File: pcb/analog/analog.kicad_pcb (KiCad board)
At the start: 2 copper layers, 70 x 70 mm, 65 parts, among them J1 USB_C_Receptacle_USB2.0, SW1 SW_Push, SW2 SW_Push, U1 SRV05-4, U2 XC6206P332MR, U3 DRV5056A3xDBZxQ1, U4 DRV5056A3xDBZxQ1, U5 DRV5056A3xDBZxQ1, U6 74AHCT1G125, U7 74AHCT1G125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

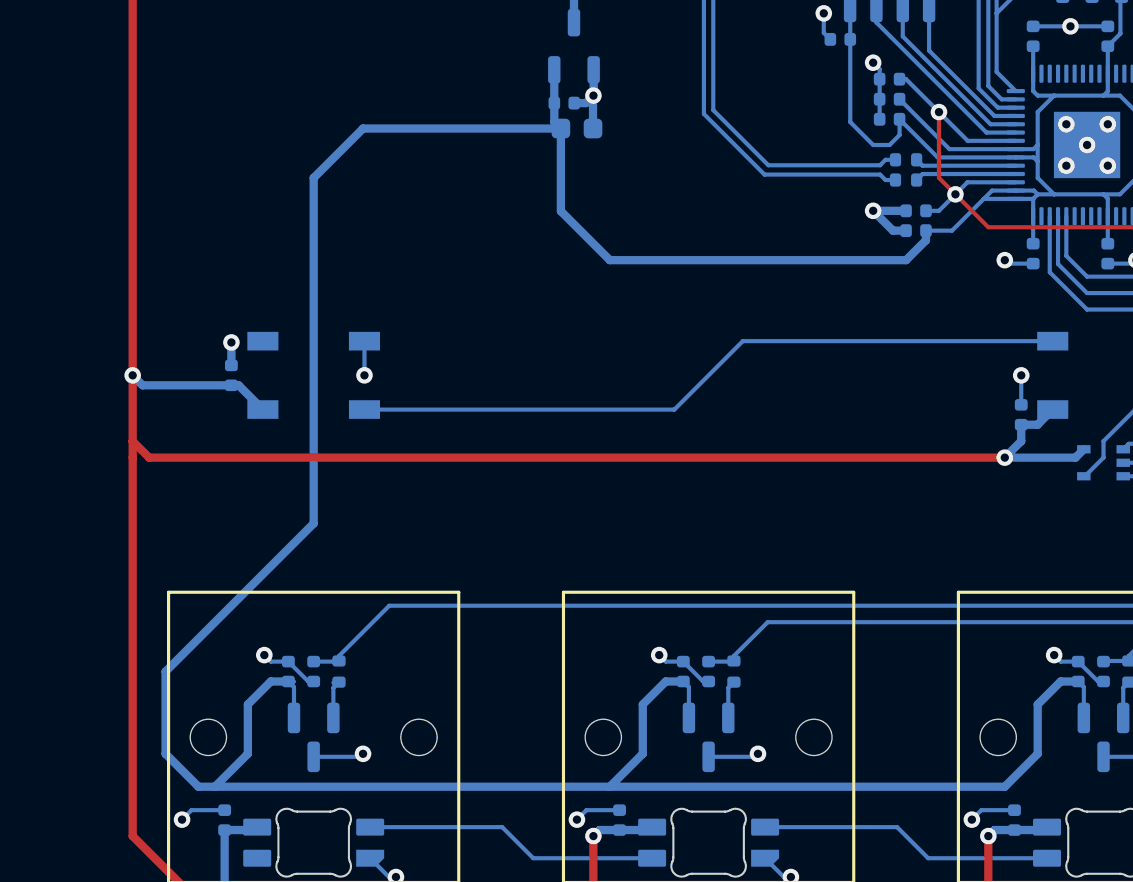
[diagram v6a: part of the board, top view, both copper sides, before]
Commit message: refactor: route analog +3v3 without going underneath LEDs just realised that it may cause some noise in the supply.
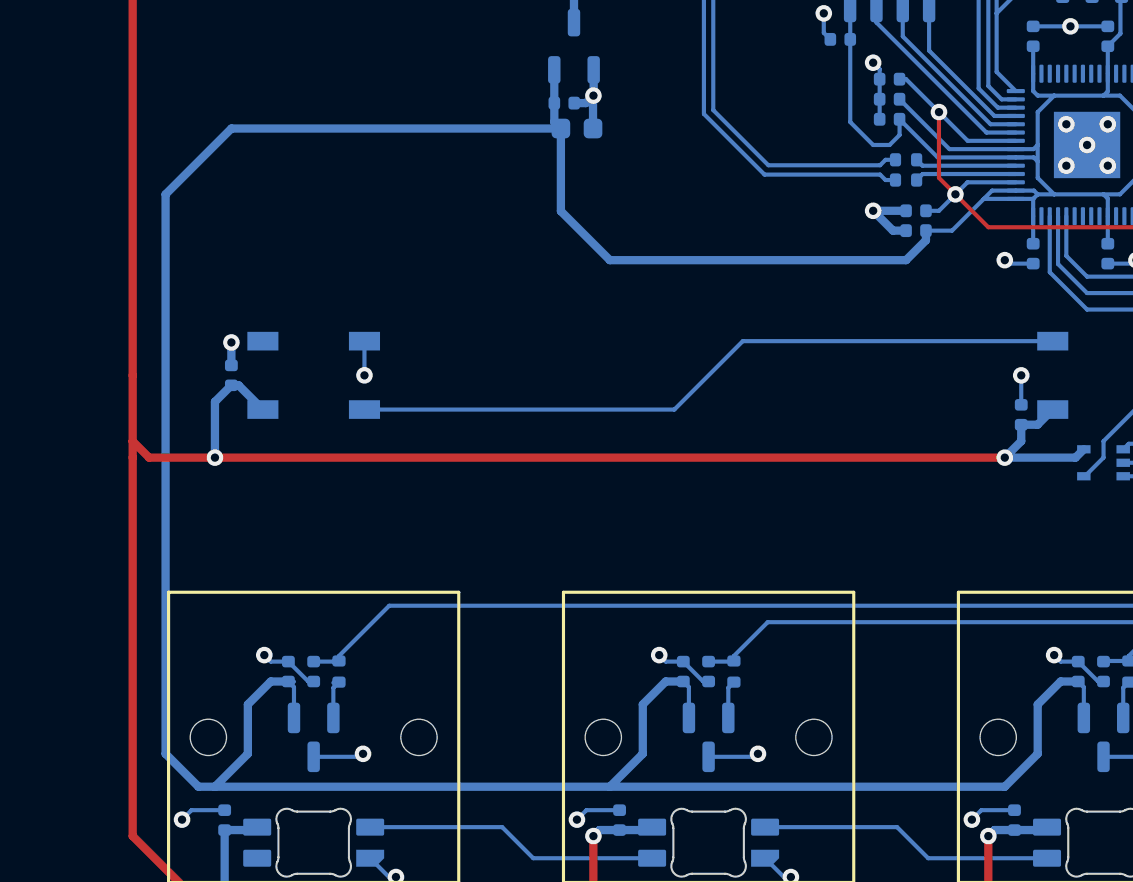
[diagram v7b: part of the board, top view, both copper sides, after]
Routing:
- net +3V3: track 212.8 -> 216.5 mm
- net +5V: track 212.3 -> 211.2 mm
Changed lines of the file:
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@@
     (stroke (width 0.1) (type default)) (layer "Edge.Cuts"))
   (segment (start 43.35625 37.665143) (end 43.358258 37.667151) (width 0.4) (layer "B.Cu") (net 1))
-  (segment (start 43.675 38.89375) (end 34.13125 38.89375) (width 0.4) (layer "B.Cu") (net 1))
   (segment (start 65.61875 42.2875) (end 64.075 42.2875) (width 0.2) (layer "B.Cu") (net 1))
   (segment (start 58.7375 39.6875) (end 57.632335 38.582335) (width 0.2) (layer "B.Cu") (net 1))
-  (segment (start 24.60625 69.05625) (end 26.19375 70.64375) (width 0.4) (layer "B.Cu") (net 1))
   (segment (start 59.53125 39.6875) (end 58.7375 39.6875) (width 0.2) (layer "B.Cu") (net 1))
-  (segment (start 31.75 57.94375) (end 24.60625 65.0875) (width 0.4) (layer "B.Cu") (net 1))
   (segment (start 66.675 38.1) (end 66.675 39.6875) (width 0.2) (layer "B.Cu") (net 1))
   (segment (start 30.8 67.325) (end 30.8 65.837505) (width 0.2) (layer "B.Cu") (net 1))
@@
   (segment (start 60.325 45.24375) (end 61.285 44.28375) (width 0.4) (layer "B.Cu") (net 1))
   (segment (start 70.05625 36.25) (end 70.05625 34.925) (width 0.2) (layer "B.Cu") (net 1))
+  (segment (start 26.19375 70.64375) (end 26.9875 70.64375) (width 0.4) (layer "B.Cu") (net 1))
   (segment (start 66.45625 36.25) (end 66.45625 34.925) (width 0.2) (layer "B.Cu") (net 1))
   (segment (start 71.6375 39.8875) (end 71.4375 39.6875) (width 0.2) (layer "B.Cu") (net 1))
   (segment (start 65.61875 40.2875) (end 61.851075 40.2875) (width 0.2) (layer "B.Cu") (net 1))
+  (segment (start 43.675 38.89375) (end 27.78125 38.89375) (width 0.4) (layer "B.Cu") (net 1))
   (segment (start 66.675 41.275) (end 67.46875 42.06875) (width 0.2) (layer "B.Cu") (net 1))
   (segment (start 71.4375 39.6875) (end 71.4375 38.1) (width 0.2) (layer "B.Cu") (net 1))
@@
   (segment (start 66.675 37.30625) (end 67.46875 37.30625) (width 0.2) (layer "B.Cu") (net 1))
   (segment (start 69.85 37.30625) (end 67.46875 37.30625) (width 0.2) (layer "B.Cu") (net 1))
+  (segment (start 27.78125 38.89375) (end 24.60625 42.06875) (width 0.4) (layer "B.Cu") (net 1))
   (segment (start 70.05625 36.25) (end 70.05625 37.1) (width 0.2) (layer "B.Cu") (net 1))
   (segment (start 65.61875 40.2875) (end 66.48125 40.2875) (width 0.2) (layer "B.Cu") (net 1))
@@
   (segment (start 65.61875 39.8875) (end 62.417962 39.8875) (width 0.2) (layer "B.Cu") (net 1))
   (segment (start 30.8 65.837505) (end 30.529995 65.5675) (width 0.2) (layer "B.Cu") (net 1))
-  (segment (start 31.75 41.275) (end 31.75 57.94375) (width 0.4) (layer "B.Cu") (net 1))
   (segment (start 62.417962 39.8875) (end 60.01125 37.480788) (width 0.2) (layer "B.Cu") (net 1))
   (segment (start 70.05625 42.275) (end 69.85 42.06875) (width 0.2) (layer "B.Cu") (net 1))
@@
   (segment (start 66.45625 43.125) (end 66.45625 44.45) (width 0.2) (layer "B.Cu") (net 1))
   (segment (start 67.46875 42.06875) (end 69.85 42.06875) (width 0.2) (layer "B.Cu") (net 1))
+  (segment (start 24.60625 69.05625) (end 26.19375 70.64375) (width 0.4) (layer "B.Cu") (net 1))
   (segment (start 66.48125 40.2875) (end 66.675 40.48125) (width 0.2) (layer "B.Cu") (net 1))
   (segment (start 64.075 42.2875) (end 62.543453 43.819047) (width 0.2) (layer "B.Cu") (net 1))
-  (segment (start 26.19375 70.64375) (end 26.9875 70.64375) (width 0.4) (layer "B.Cu") (net 1))
   (segment (start 67.46875 37.30625) (end 66.675 38.1) (width 0.2) (layer "B.Cu") (net 1))
   (segment (start 28.575 69.05625) (end 28.575 66.675) (width 0.4) (layer "B.Cu") (net 1))
@@
   (segment (start 68.890937 67.315937) (end 68.9 67.325) (width 0.2) (layer "B.Cu") (net 1))
   (segment (start 43.358258 38.577008) (end 43.675 38.89375) (width 0.4) (layer "B.Cu") (net 1))
-  (segment (start 24.60625 65.0875) (end 24.60625 69.05625) (width 0.4) (layer "B.Cu") (net 1))
   (segment (start 66.45625 42.2875) (end 66.675 42.06875) (width 0.2) (layer "B.Cu") (net 1))
+  (segment (start 24.60625 42.06875) (end 24.60625 69.05625) (width 0.4) (layer "B.Cu") (net 1))
   (segment (start 64.475 41.8875) (end 64.075 42.2875) (width 0.2) (layer "B.Cu") (net 1))
   (segment (start 57.632335 38.582335) (end 57.632335 34.59375) (width 0.2) (layer "B.Cu") (net 1))
@@
   (segment (start 72.49375 39.8875) (end 74.661593 39.8875) (width 0.2) (layer "B.Cu") (net 1))
   (segment (start 26.9875 70.64375) (end 46.0375 70.64375) (width 0.4) (layer "B.Cu") (net 1))
-  (segment (start 34.13125 38.89375) (end 31.75 41.275) (width 0.4) (layer "B.Cu") (net 1))
   (segment (start 48.7325 65.5675) (end 49.579995 65.5675) (width 0.4) (layer "B.Cu") (net 1))
   (segment (start 70.05625 44.45) (end 70.05625 43.125) (width 0.2) (layer "B.Cu") (net 1))
@@
   (segment (start 76.670543 39.959446) (end 76.670543 40.93645) (width 0.2) (layer "B.Cu") (net 2))
   (segment (start 45.24375 76.2) (end 45.24375 73.025) (width 0.4) (layer "F.Cu") (net 3))
+  (segment (start 26.9875 54.76875) (end 65.0875 54.76875) (width 0.4) (layer "F.Cu") (net 3))
   (segment (start 23.01875 54.76875) (end 23.01875 73.025) (width 0.4) (layer "F.Cu") (net 3))
   (segment (start 23.01875 29.36875) (end 23.01875 50.8) (width 0.4) (layer "F.Cu") (net 3))
@@
   (segment (start 23.01875 50.8) (end 23.01875 53.975) (width 0.4) (layer "F.Cu") (net 3))
   (segment (start 40.48125 25.4) (end 26.9875 25.4) (width 0.4) (layer "F.Cu") (net 3))
-  (segment (start 23.8125 54.76875) (end 65.0875 54.76875) (width 0.4) (layer "F.Cu") (net 3))
   (segment (start 23.01875 53.975) (end 23.01875 54.76875) (width 0.4) (layer "F.Cu") (net 3))
   (segment (start 26.9875 25.4) (end 23.01875 29.36875) (width 0.4) (layer "F.Cu") (net 3))
   (segment (start 64.29375 76.2) (end 75.40625 76.2) (width 0.4) (layer "F.Cu") (net 3))
+  (segment (start 23.8125 54.76875) (end 26.9875 54.76875) (width 0.4) (layer "F.Cu") (net 3))
   (segment (start 23.01875 53.975) (end 23.8125 54.76875) (width 0.4) (layer "F.Cu") (net 3))
   (segment (start 64.29375 76.2) (end 64.29375 73.025) (width 0.4) (layer "F.Cu") (net 3))
   (via (at 45.24375 73.025) (size 0.8) (drill 0.4) (layers "F.Cu" "B.Cu") (net 3))
-  (via (at 23.01875 50.8) (size 0.8) (drill 0.4) (layers "F.Cu" "B.Cu") (net 3))
+  (via (at 26.9875 54.76875) (size 0.8) (drill 0.4) (layers "F.Cu" "B.Cu") (net 3))
   (via (at 26.9875 76.2) (size 0.8) (drill 0.4) (layers "F.Cu" "B.Cu") (net 3))
   (via (at 65.0875 54.76875) (size 0.8) (drill 0.4) (layers "F.Cu" "B.Cu") (net 3))
@@
   (segment (start 65.88125 53.18125) (end 65.88125 53.975) (width 0.4) (layer "B.Cu") (net 3))
   (segment (start 46.0375 29.36875) (end 44.30625 27.6375) (width 0.4) (layer "B.Cu") (net 3))
-  (segment (start 23.01875 50.8) (end 23.49875 51.28) (width 0.4) (layer "B.Cu") (net 3))
   (segment (start 49.625 29.36875) (end 46.0375 29.36875) (width 0.4) (layer "B.Cu") (net 3))
-  (segment (start 23.49875 51.28) (end 27.780361 51.28) (width 0.4) (layer "B.Cu") (net 3))
   (segment (start 44.30625 27.6375) (end 44.30625 25.4) (width 0.4) (layer "B.Cu") (net 3))
   (segment (start 28.883694 72.733806) (end 29.025 72.5925) (width 0.4) (layer "B.Cu") (net 3))
@@
   (segment (start 65.555346 72.733806) (end 66.983694 72.733806) (width 0.4) (layer "B.Cu") (net 3))
   (segment (start 65.88125 53.18125) (end 66.66875 53.18125) (width 0.4) (layer "B.Cu") (net 3))
+  (segment (start 26.9875 52.072861) (end 26.9875 54.76875) (width 0.4) (layer "B.Cu") (net 3))
   (segment (start 27.455346 72.733806) (end 28.883694 72.733806) (width 0.4) (layer "B.Cu") (net 3))
   (segment (start 64.584944 72.733806) (end 64.29375 73.025) (width 0.4) (layer "B.Cu") (net 3))
@@
   (segment (start 68.498352 54.76875) (end 65.0875 54.76875) (width 0.4) (layer "B.Cu") (net 3))
   (segment (start 66.983694 72.733806) (end 67.125 72.5925) (width 0.4) (layer "B.Cu") (net 3))
+  (segment (start 27.780361 51.28) (end 26.9875 52.072861) (width 0.4) (layer "B.Cu") (net 3))
   (segment (start 46.0375 29.36875) (end 44.309018 31.097232) (width 0.4) (layer "B.Cu") (net 3))
   (segment (start 45.24375 73.025) (end 45.534944 72.733806) (width 0.4) (layer "B.Cu") (net 3))

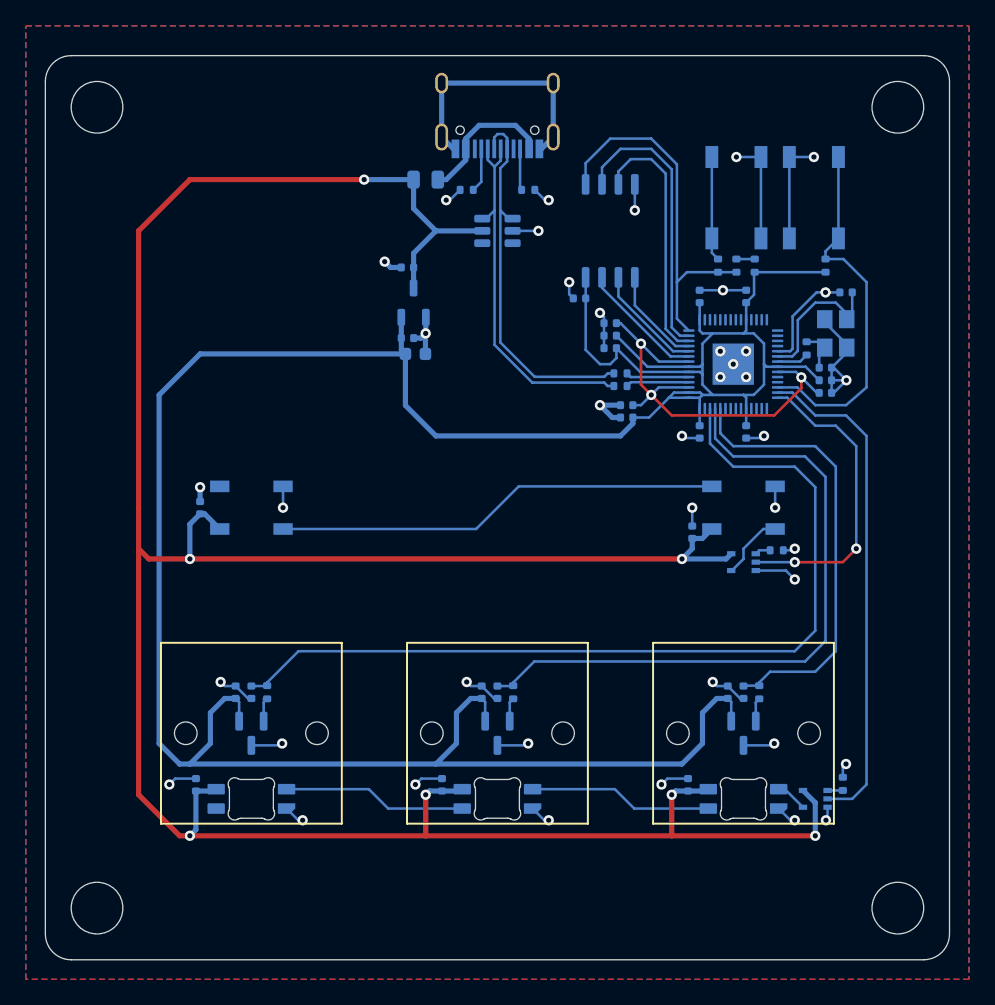
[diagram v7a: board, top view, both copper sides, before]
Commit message: feat: add bottom piece cutouts for pcb buttons
I ended up moving the buttons slightly so it appears more evenly spaced.

There's also silkscreen labels indicating which buttons they are, whcih should make instructions a bit easier.
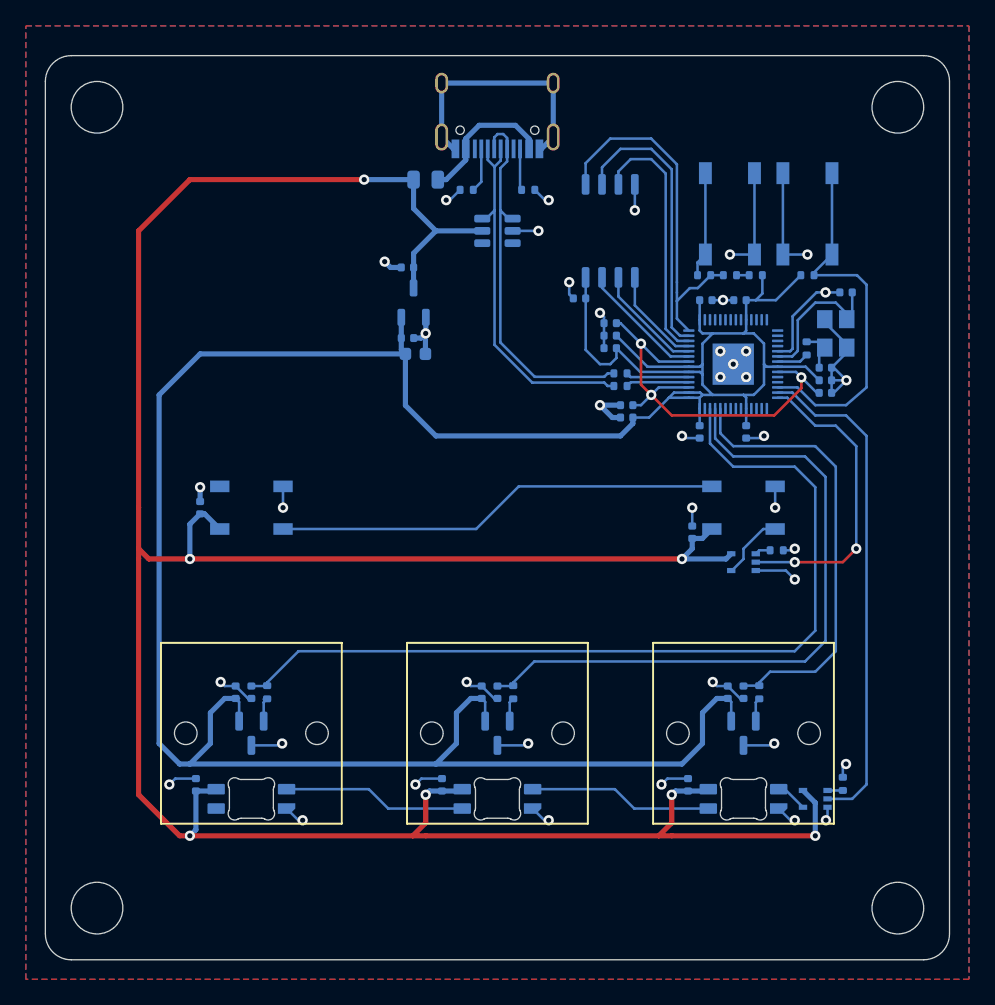
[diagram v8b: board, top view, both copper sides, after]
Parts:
- moved R12 1.58 mm to (74.8, 32.8), turned to 0 degrees
- moved SW1 1.35 mm to (74.8, 28.1)
- moved SW2 1.35 mm to (68.8, 28.1)
- moved R14 1.31 mm to (66.8, 32.8), turned to 0 degrees
- moved R13 0.89 mm to (68.8, 32.8), turned to 180 degrees
- moved R10 0.75 mm to (70.8, 32.8), turned to 180 degrees
- moved C22 0.56 mm to (69.6, 34.7), turned to 180 degrees
- moved C23 0.56 mm to (66.9, 34.7), turned to 0 degrees
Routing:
- net GND: track 122.0 -> 120.1 mm
- net +5V: track 211.2 -> 212.0 mm
- net +3V3: track 216.5 -> 216.0 mm
- net Q_SEL: track 28.5 -> 28.0 mm
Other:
- board text added: "RST"
- board text added: "SEL"
